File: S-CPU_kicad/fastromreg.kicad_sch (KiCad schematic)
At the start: 24 parts

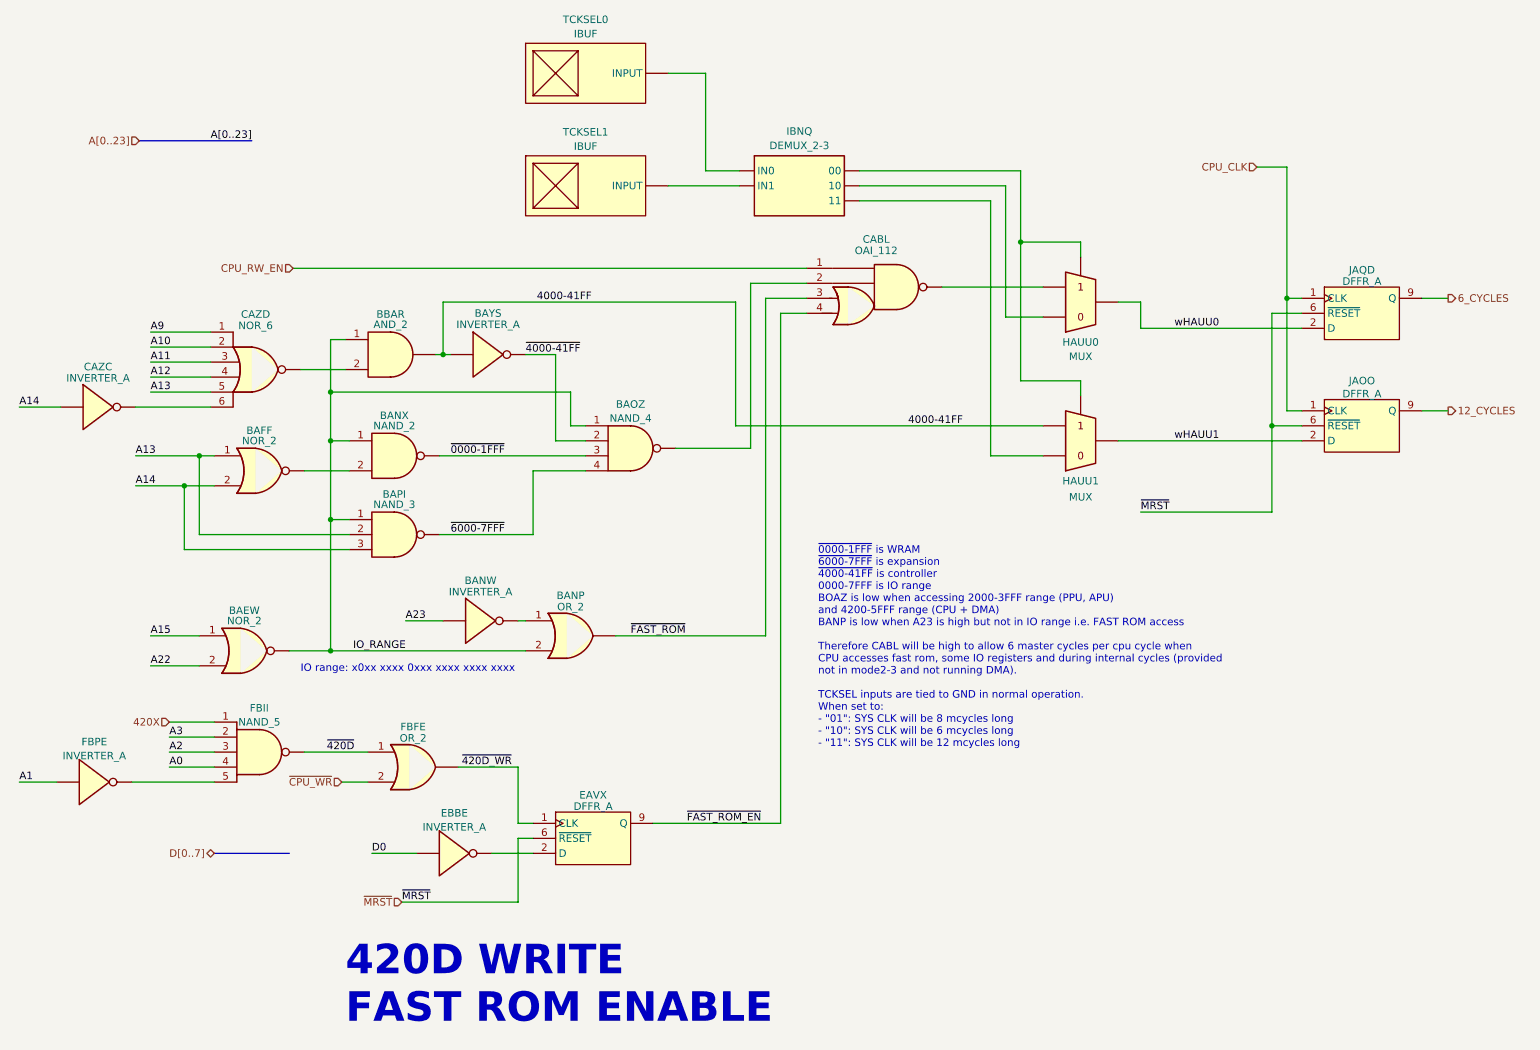
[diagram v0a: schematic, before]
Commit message: Fixed VAWR which should have been an SR DFF (to fix issue #3 raised in github)
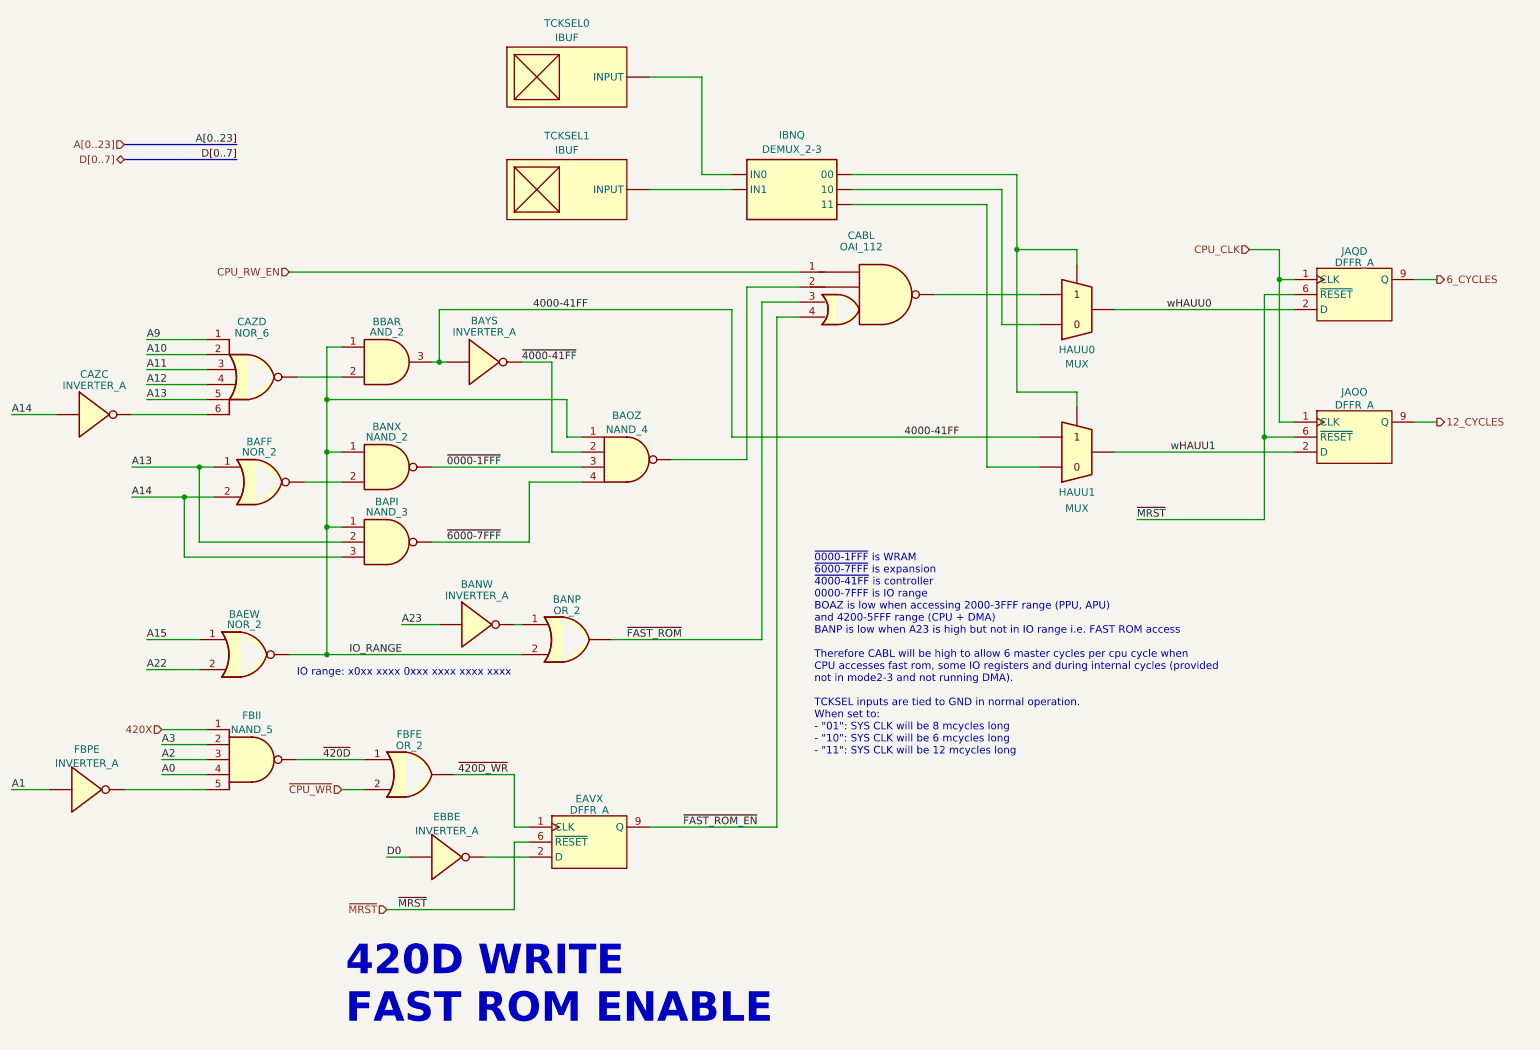
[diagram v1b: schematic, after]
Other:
- moved on the sheet: BAEW, BAFF, BANP, BANW, BANX, BAOZ, BAPI, BAYS, CAZC, CAZD, EAVX, EBBE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
